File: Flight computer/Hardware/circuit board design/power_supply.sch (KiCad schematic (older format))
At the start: 18 parts, among them J2 USB_B_Micro, J3 Conn_01x02, Q1 Q_PMOS_DGS, U9 TPS61200DRC

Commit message: added in LDO based power supply
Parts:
- removed Q?: Q_PMOS_DGS, Package_TO_SOT_SMD:SOT-23, symbol Device:Q_PMOS_DGS
- removed R?: 10K, Resistor_SMD:R_0603_1608Metric, symbol Device:R
- added C?: 10nF, Capacitor_SMD:C_0603_1608Metric, symbol Device:C
- added D3: DFLS130L, symbol flight-computer:DFLS130L
- added U14: MAX40200AUK, Package_TO_SOT_SMD:SOT-23-5, symbol Analog_Switch:MAX40200AUK
- added U15: LD3985G33R_TSOT23, Package_TO_SOT_SMD:TSOT-23-5, symbol Regulator_Linear:LD3985G33R_TSOT23
- gave numbers to parts that had none: 1
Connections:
- net labels added: Vdrive
- wire segments 74 -> 82
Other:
- note added: "1A Ideal Diode with Ultra-Low Voltage Drop"
- moved on the sheet: J2, J4

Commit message: added screw terminal symbols and anotated power supply page
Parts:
- removed C81, C83, C84: 10uF, Capacitor_SMD:C_0603_1608Metric, symbol Device:C
- removed C82, C85: 100nF, Capacitor_SMD:C_0603_1608Metric, symbol Device:C
- removed J3: Conn_01x02, Connector_PinHeader_1.00mm:PinHeader_1x02_P1.00mm_Vertical, symbol Connector_Generic:Conn_01x02
- removed L23: 2.2uH, Inductor_SMD:L_Taiyo-Yuden_NR-30xx, symbol Device:L
- removed Q1: Q_PMOS_DGS, Package_TO_SOT_SMD:SOT-23, symbol Device:Q_PMOS_DGS
- removed R10: 180K, Resistor_SMD:R_0603_1608Metric, symbol Device:R
- removed R11: 10K, Resistor_SMD:R_0603_1608Metric, symbol Device:R
- removed R7, R8: 100K, Resistor_SMD:R_0603_1608Metric, symbol Device:R
- removed R9: 1M, Resistor_SMD:R_0603_1608Metric, symbol Device:R
- removed U9: TPS61200DRC, Package_SON:Texas_S-PVSON-N10_ThermalVias, symbol Regulator_Switching:TPS61200DRC
- added C35, C36: 1uf, Capacitor_SMD:C_0603_1608Metric, symbol Device:C
- added C9: 100nF, Capacitor_SMD:C_0603_1608Metric, symbol Device:C
- added Q2: Q_PMOS_DGS, Package_TO_SOT_SMD:SOT-23, symbol Device:Q_PMOS_DGS
- added R27: 10K, Resistor_SMD:R_0603_1608Metric, symbol Device:R
- added R28, R29: 100K, Resistor_SMD:R_0603_1608Metric, symbol Device:R
- gave numbers to parts that had none: 1
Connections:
- net labels removed: VMEM
- wire segments 82 -> 50
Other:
- note added: "1A Ideal Diode with Ultra-Low Voltage Drop.\n43mV drop at 500mA draw"
- note added: "3.6V-4.2V Li-po input. Needs to be\nregulated down to 3.3V cmos"
- note added: "May have to increase \nthe smoothing caps to 10uF \nfor stronger effect."
- note added: "The maximum possible voltage drop due to diode \nand LDO regulator is 173mV, leaving plenty of \nleeway to bring it down to 3.3V CMOS level."
- note added: "Ultra low drop out voltage regulator.\n140mV drop at max current of 150mA."
- note removed: "1A Ideal Diode with Ultra-Low Voltage Drop"
- moved on the sheet: C34, D3, J2, J4, U14, U15

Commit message: set up the PCB to fit formfactor
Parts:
- D3: footprint (none) -> Diode_SMD:D_PowerDI-123
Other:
- note added: "The maximum possible voltage drop(from 3.6V input) due to diode \nand LDO regulator is 173mV, leaving plenty of \nleeway to bring it down to 3.3V CMOS level."
- note removed: "The maximum possible voltage drop due to diode \nand LDO regulator is 173mV, leaving plenty of \nleeway to bring it down to 3.3V CMOS level."
- moved on the sheet: C34, C35, C36, C9, D3, J2, J4, R27, R28, R29, U14, U15

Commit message: changed the footprint for 220 nH inductor and removed the circuit for low power voltage measurments
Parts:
- removed C9: 100nF, Capacitor_SMD:C_0603_1608Metric, symbol Device:C
- removed Q2: Q_PMOS_DGS, Package_TO_SOT_SMD:SOT-23, symbol Device:Q_PMOS_DGS
- removed R27: 10K, Resistor_SMD:R_0603_1608Metric, symbol Device:R
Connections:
- net labels removed: PWR_MEASURE
- wire segments 50 -> 43
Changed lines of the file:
@@
 $EndComp
-Wire Wire Line
-	1400 4000 2000 4000
-Text HLabel 1400 4000 0    50   Input ~ 0
-PWR_MEASURE
-Connection ~ 2600 4000
-Wire Wire Line
-	2600 4000 2300 4000
-Wire Wire Line
-	3050 4800 3050 4950
-Connection ~ 3050 4800
-Wire Wire Line
-	1400 4800 3050 4800
-Wire Wire Line
-	3050 4750 3050 4800
-$Comp
-L Device:C C9
-U 1 1 5D7595ED
-P 2150 4000
-F 0 "C9" V 2402 4000 50  0000 C CNN
-F 1 "100nF" V 2311 4000 50  0000 C CNN
-F 2 "Capacitor_SMD:C_0603_1608Metric" H 2188 3850 50  0001 C CNN
-F 3 "~" H 2150 4000 50  0001 C CNN
-	1    2150 4000
-	0    -1   -1   0
-$EndComp
-Wire Wire Line
-	2750 4000 2600 4000
-Wire Wire Line
-	3050 4200 3050 4450
-Wire Wire Line
-	3050 3800 3050 3300
-Wire Wire Line
-	2600 3900 2600 4000
-$Comp
-L Device:Q_PMOS_DGS Q2
-U 1 1 5D7595FB
-P 2950 4000
-F 0 "Q2" H 3156 3954 50  0000 L CNN
-F 1 "Q_PMOS_DGS" H 3156 4045 50  0000 L CNN
-F 2 "Package_TO_SOT_SMD:SOT-23" H 3150 4100 50  0001 C CNN
-F 3 "~" H 2950 4000 50  0001 C CNN
-	1    2950 4000
-	1    0    0    1
-$EndComp
-$Comp
-L Device:R R27
-U 1 1 5D759605
-P 2600 3750
-F 0 "R27" H 2670 3796 50  0000 L CNN
-F 1 "10K" H 2670 3705 50  0000 L CNN
-F 2 "Resistor_SMD:R_0603_1608Metric" V 2530 3750 50  0001 C CNN
-F 3 "~" H 2600 3750 50  0001 C CNN
-	1    2600 3750
-	1    0    0    -1
-$EndComp
-Text HLabel 1400 4800 0    50   Output ~ 0
-PWR_BVOLTS
 Wire Wire Line
 	3050 5350 3050 5250
@@
 	1    0    0    -1
 $EndComp
-Connection ~ 3050 3300
-Wire Wire Line
-	3050 3300 3550 3300
-Wire Wire Line
-	2600 3600 2600 3300
-Connection ~ 2600 3300
 Wire Wire Line
 	3550 3150 3550 3300
@@
 Connection ~ 2200 3300
 Wire Wire Line
-	2200 3300 2600 3300
-Wire Wire Line
 	1750 3300 2200 3300
-Wire Wire Line
-	2600 3300 3050 3300
 Text Notes 7350 3900 0    50   ~ 0
 May have to increase \nthe smoothing caps to 10uF \nfor stronger effect.
@@
 Text Notes 6250 5000 0    50   ~ 0
 The maximum possible voltage drop(from 3.6V input) due to diode \nand LDO regulator is 173mV, leaving plenty of \nleeway to bring it down to 3.3V CMOS level.
+Wire Wire Line
+	3050 3300 3550 3300
+Connection ~ 3050 3300
+Text HLabel 1400 4800 0    50   Output ~ 0
+PWR_BVOLTS
+Wire Wire Line
+	3050 4750 3050 4800
+Wire Wire Line
+	3050 4800 3050 4950
+Connection ~ 3050 4800
+Wire Wire Line
+	1400 4800 3050 4800
+Wire Wire Line
+	2200 3300 3050 3300
+Wire Wire Line
+	3050 3300 3050 4450
 $EndSCHEMATC

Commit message: put in an arming switch
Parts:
- J4: footprint Connector_PinHeader_1.00mm:PinHeader_1x02_P1.00mm_Vertical -> Connector_PinHeader_2.54mm:PinHeader_1x02_P2.54mm_Vertical
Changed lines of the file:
@@
 F 0 "J4" H 1468 3517 50  0000 C CNN
 F 1 "Conn_01x02" H 1468 3426 50  0000 C CNN
-F 2 "Connector_PinHeader_1.00mm:PinHeader_1x02_P1.00mm_Vertical" H 1550 3300 50  0001 C CNN
+F 2 "Connector_PinHeader_2.54mm:PinHeader_1x02_P2.54mm_Vertical" H 1550 3300 50  0001 C CNN
 F 3 "~" H 1550 3300 50  0001 C CNN
 	1    1550 3300

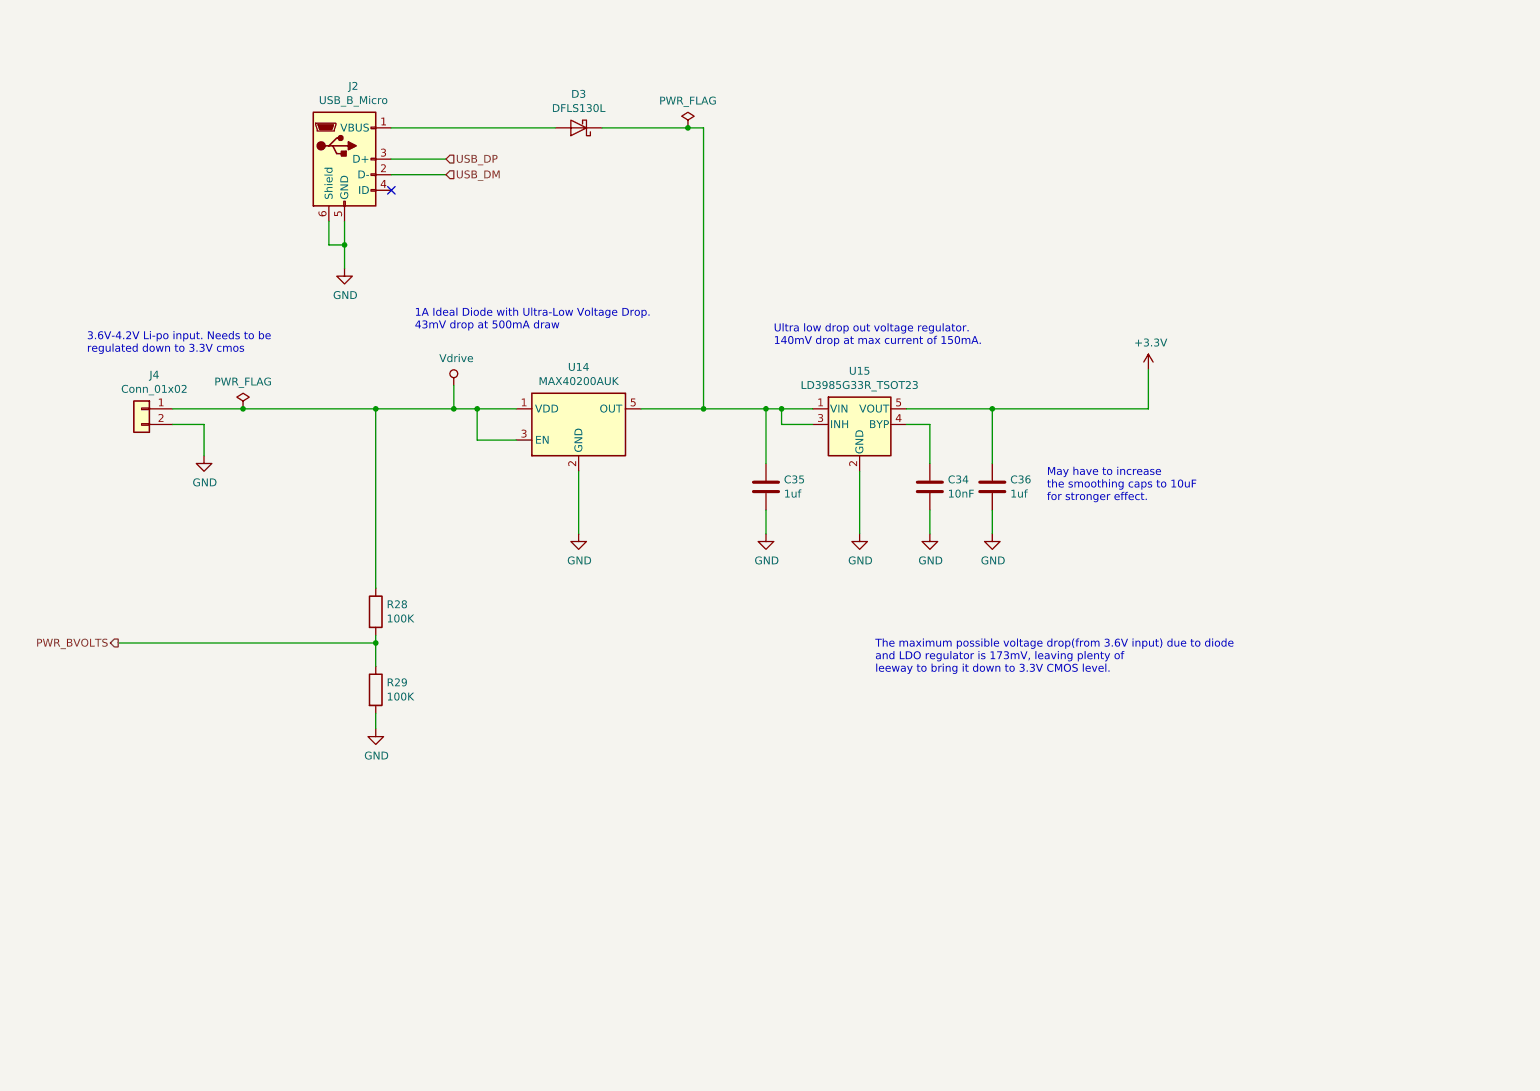
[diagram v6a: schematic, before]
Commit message: Added the USB protection IC
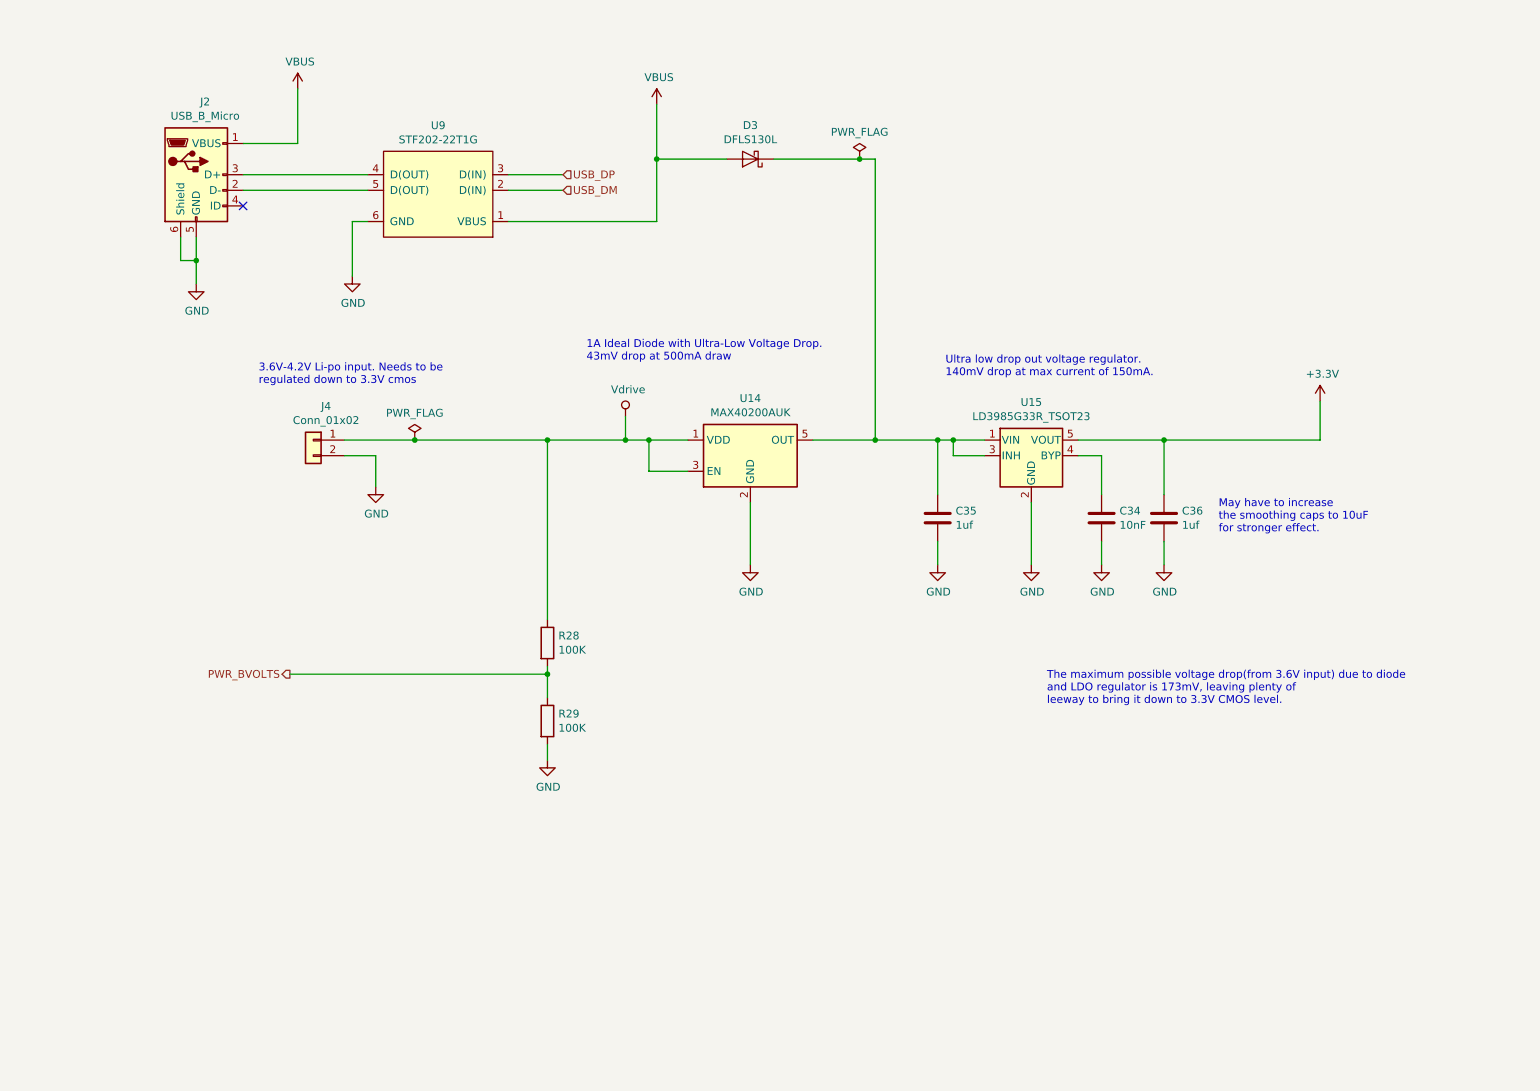
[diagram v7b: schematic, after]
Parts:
- added U9: STF202-22T1G, Package_SO:TSOP-6_1.65x3.05mm_P0.95mm, symbol flight-computer:STF202-22T1G
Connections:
- net GND: now also U9.6 (GND)
- net USB_DM: now also U9.2 (D(IN)); no longer J2.2 (D-)
- net USB_DP: now also U9.3 (D(IN)); no longer J2.3 (D+)
- net VBUS: now reaches D3.2 (A), J2.1 (VBUS)
- net VBUS: now also U9.1 (VBUS)
- new net: J2.3 (D+), U9.4 (D(OUT))
- new net: J2.2 (D-), U9.5 (D(OUT))
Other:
- moved on the sheet: C34, C35, C36, D3, J2, J4, R28, R29, U14, U15

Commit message: added the arming switch. Changed foot print of lipo connector to JST
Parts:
- J4: footprint Connector_PinHeader_2.54mm:PinHeader_1x02_P2.54mm_Vertical -> Connector_JST:JST_PH_B2B-PH-K_1x02_P2.00mm_Vertical
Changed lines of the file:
@@
 F 0 "J4" H 2568 3717 50  0000 C CNN
 F 1 "Conn_01x02" H 2568 3626 50  0000 C CNN
-F 2 "Connector_PinHeader_2.54mm:PinHeader_1x02_P2.54mm_Vertical" H 2650 3500 50  0001 C CNN
+F 2 "Connector_JST:JST_PH_B2B-PH-K_1x02_P2.00mm_Vertical" H 2650 3500 50  0001 C CNN
 F 3 "~" H 2650 3500 50  0001 C CNN
 	1    2650 3500
@@
 $EndComp
 Wire Wire Line
-	4150 5550 4150 5450
-$Comp
-L power:GND #PWR0111
-U 1 1 5D759611
-P 4150 5550
-F 0 "#PWR0111" H 4150 5300 50  0001 C CNN
-F 1 "GND" H 4155 5377 50  0000 C CNN
-F 2 "" H 4150 5550 50  0001 C CNN
-F 3 "" H 4150 5550 50  0001 C CNN
-	1    4150 5550
-	1    0    0    -1
-$EndComp
-$Comp
-L Device:R R29
-U 1 1 5D75961B
-P 4150 5300
-F 0 "R29" H 4220 5346 50  0000 L CNN
-F 1 "100K" H 4220 5255 50  0000 L CNN
-F 2 "Resistor_SMD:R_0603_1608Metric" V 4080 5300 50  0001 C CNN
-F 3 "~" H 4150 5300 50  0001 C CNN
-	1    4150 5300
-	1    0    0    -1
-$EndComp
-$Comp
-L Device:R R28
-U 1 1 5D759625
-P 4150 4800
-F 0 "R28" H 4220 4846 50  0000 L CNN
-F 1 "100K" H 4220 4755 50  0000 L CNN
-F 2 "Resistor_SMD:R_0603_1608Metric" V 4080 4800 50  0001 C CNN
-F 3 "~" H 4150 4800 50  0001 C CNN
-	1    4150 4800
-	1    0    0    -1
-$EndComp
-Wire Wire Line
 	4650 3350 4650 3500
 $Comp
@@
 	4150 3500 4650 3500
 Connection ~ 4150 3500
-Text HLabel 2500 5000 0    50   Output ~ 0
-PWR_BVOLTS
-Wire Wire Line
-	4150 4950 4150 5000
-Wire Wire Line
-	4150 5000 4150 5150
-Connection ~ 4150 5000
-Wire Wire Line
-	2500 5000 4150 5000
 Wire Wire Line
 	3300 3500 4150 3500
-Wire Wire Line
-	4150 3500 4150 4650
 $Comp
 L Connector:USB_B_Micro J?
@@
 USB_DP
 Wire Wire Line
-	2200 1900 3000 1900
-Wire Wire Line
-	3000 1800 2200 1800
-Wire Wire Line
 	3000 2100 2900 2100
 Wire Wire Line
@@
 	2200 1600 2550 1600
 Wire Wire Line
-	3900 2100 4850 2100
-Wire Wire Line
 	4850 2100 4850 1700
 Wire Wire Line
@@
 	1    0    0    -1
 $EndComp
+Wire Wire Line
+	4150 3500 4150 4650
+Wire Wire Line
+	2500 5000 4150 5000
+Connection ~ 4150 5000
+Wire Wire Line
+	4150 5000 4150 5150
+Wire Wire Line
+	4150 4950 4150 5000
+Text HLabel 2500 5000 0    50   Output ~ 0
+PWR_BVOLTS
+$Comp
+L Device:R R28
+U 1 1 5D759625
+P 4150 4800
+F 0 "R28" H 4220 4846 50  0000 L CNN
+F 1 "100K" H 4220 4755 50  0000 L CNN
+F 2 "Resistor_SMD:R_0603_1608Metric" V 4080 4800 50  0001 C CNN
+F 3 "~" H 4150 4800 50  0001 C CNN
+	1    4150 4800
+	1    0    0    -1
+$EndComp
+$Comp
+L Device:R R29
+U 1 1 5D75961B
+P 4150 5300
+F 0 "R29" H 4220 5346 50  0000 L CNN
+F 1 "100K" H 4220 5255 50  0000 L CNN
+F 2 "Resistor_SMD:R_0603_1608Metric" V 4080 5300 50  0001 C CNN
+F 3 "~" H 4150 5300 50  0001 C CNN
+	1    4150 5300
+	1    0    0    -1
+$EndComp
+$Comp
+L power:GND #PWR0111
+U 1 1 5D759611
+P 4150 5550
+F 0 "#PWR0111" H 4150 5300 50  0001 C CNN
+F 1 "GND" H 4155 5377 50  0000 C CNN
+F 2 "" H 4150 5550 50  0001 C CNN
+F 3 "" H 4150 5550 50  0001 C CNN
+	1    4150 5550
+	1    0    0    -1
+$EndComp
+Wire Wire Line
+	4150 5550 4150 5450
+Wire Wire Line
+	3900 2100 4850 2100
+Wire Wire Line
+	2200 1900 3000 1900
+Wire Wire Line
+	3000 1800 2200 1800
 $EndSCHEMATC
